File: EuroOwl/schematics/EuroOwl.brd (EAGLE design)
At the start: 100 x 99.8 mm, 119 parts, among them IC1 QUAD_OPAMPD, IC2 QUAD_OPAMPD, IC3 TL072D, Q900 BC846, Q901 BC846, X1 USBPTH-VERTICAL

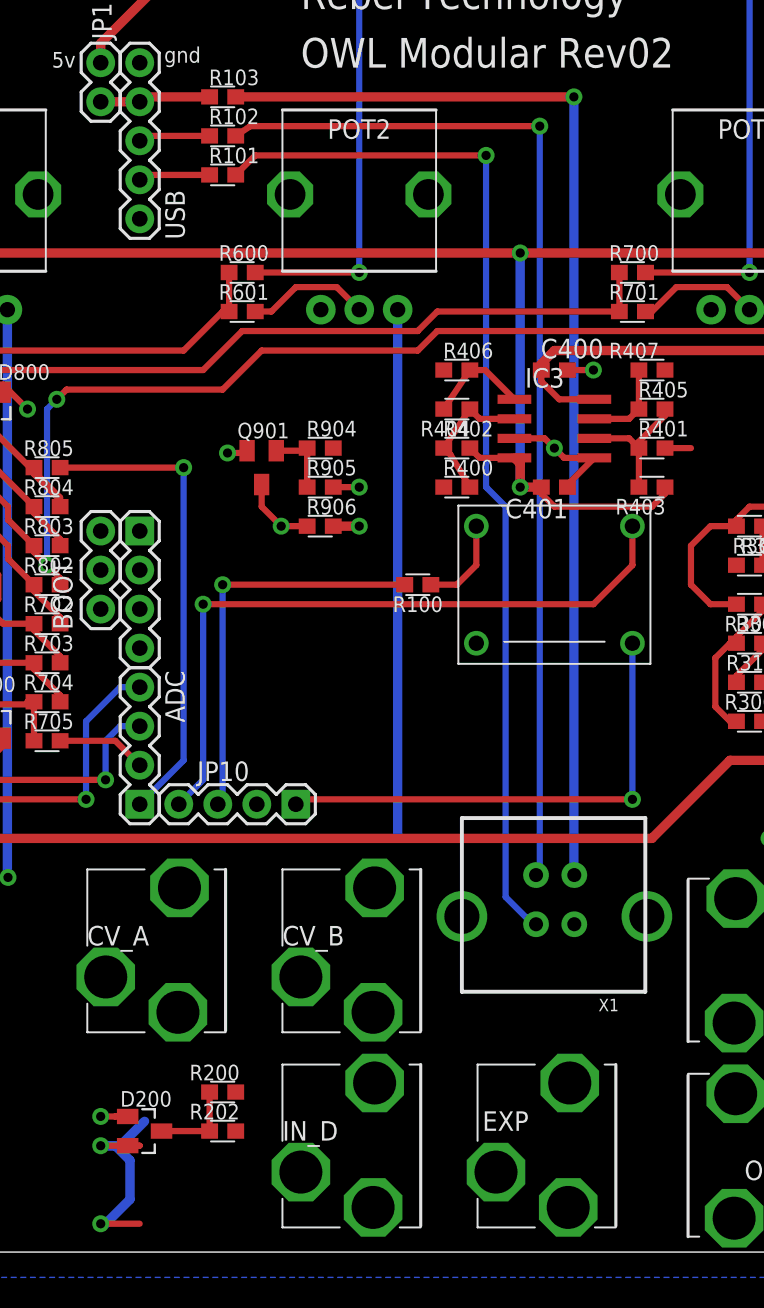
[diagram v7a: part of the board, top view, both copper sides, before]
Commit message: moved USB connector down
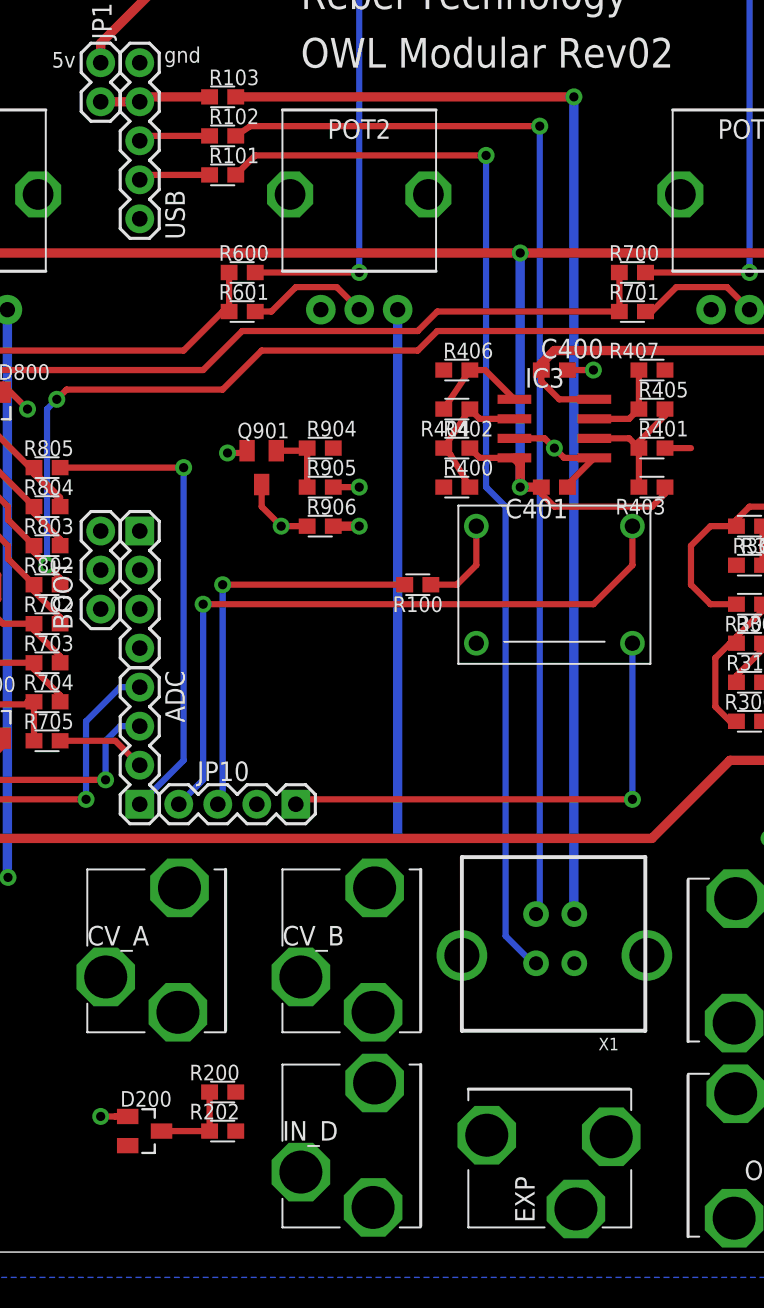
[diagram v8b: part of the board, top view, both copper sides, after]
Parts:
- moved X1 2.54 mm to (50.8, 20.3)
- turned EXP to 90 degrees
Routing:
- net +3V3: track 209.9 -> 193.1 mm, vias 11 -> 9
- net N$52: track 68.8 -> 71.5 mm
- net N$51: track 68.3 -> 70.9 mm
- net N$54: track 72.7 -> 75.2 mm
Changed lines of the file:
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@@
 <element name="OUT_L" library="Rebel" package="CON-LUMBERG_1502_03" value="CON-LUMBERG_1502_03" x="91.44" y="20.32" rot="R180"/>
 <element name="OUT_R" library="Rebel" package="CON-LUMBERG_1502_03" value="CON-LUMBERG_1502_03" x="91.44" y="7.62" rot="R180"/>
-<element name="EXP" library="Rebel" package="CON-LUMBERG_1502_03" value="CON-LUMBERG_1502_03" x="50.8" y="7.62" smashed="yes">
-<attribute name="NAME" x="46.1175" y="8.905" size="1.27" layer="25" font="vector"/>
+<element name="EXP" library="Rebel" package="CON-LUMBERG_1502_03" value="CON-LUMBERG_1502_03" x="50.8" y="7.62" smashed="yes" rot="R90">
+<attribute name="NAME" x="49.515" y="2.9375" size="1.27" layer="25" font="vector" rot="R90"/>
 </element>
 <element name="POT5" library="Rebel" package="POT-ALPS-RK09L1140" value="POT-ALPS-RK09L1140" x="12.7" y="95.25" locked="yes"/>
@@
 <attribute name="NAME" x="78.1685" y="12.192" size="1.016" layer="25"/>
 </element>
-<element name="X1" library="SparkFun" package="USB-B-PTH-VERTICAL" value="USBPTH-VERTICAL" x="50.8" y="22.86"/>
+<element name="X1" library="SparkFun" package="USB-B-PTH-VERTICAL" value="USBPTH-VERTICAL" x="50.8" y="20.32"/>
 <element name="R101" library="Rebel" package="0603" value="22R" x="29.21" y="71.12" smashed="yes">
 <attribute name="NAME" x="28.321" y="71.882" size="1.016" layer="25"/>
@@
 <wire x1="73.72" y1="44.45" x2="73.72" y2="46.99" width="0" layer="19" extent="1-1"/>
 <wire x1="75.88" y1="55.71" x2="71.97" y2="50.8" width="0" layer="19" extent="1-1"/>
-<wire x1="52.0954" y1="22.352" x2="62.6" y2="24.02" width="0" layer="19" extent="1-1"/>
+<wire x1="52.0954" y1="19.812" x2="62.6" y2="24.02" width="0" layer="19" extent="1-1"/>
 <wire x1="62.6" y1="11.32" x2="67.3" y2="21.72" width="0" layer="19" extent="1-1"/>
 <wire x1="90.54" y1="11.32" x2="90.54" y2="24.02" width="0" layer="19" extent="1-1"/>
 <wire x1="80.96" y1="6.52" x2="90.54" y2="11.32" width="0" layer="19" extent="1-1"/>
 <wire x1="77.1525" y1="8.89" x2="80.96" y2="6.52" width="0" layer="19" extent="1-1"/>
-<wire x1="51.7" y1="3.92" x2="62.6" y2="11.32" width="0" layer="19" extent="1-1"/>
-<wire x1="47" y1="6.22" x2="51.7" y2="3.92" width="0" layer="19" extent="1-1"/>
-<wire x1="39" y1="3.92" x2="47" y2="6.22" width="0" layer="19" extent="1-1"/>
+<wire x1="54.5" y1="8.52" x2="62.6" y2="11.32" width="0" layer="19" extent="1-1"/>
+<wire x1="52.2" y1="3.82" x2="54.5" y2="8.52" width="0" layer="19" extent="1-1"/>
+<wire x1="39" y1="3.92" x2="52.2" y2="3.82" width="0" layer="19" extent="1-1"/>
 <wire x1="34.3" y1="6.22" x2="39" y2="3.92" width="0" layer="19" extent="1-1"/>
 <wire x1="39" y1="16.62" x2="34.3" y2="6.22" width="0" layer="19" extent="1-1"/>
@@
 <wire x1="36.41" y1="48.26" x2="38.1" y2="48.26" width="0.6096" layer="1"/>
 <via x="38.1" y="48.26" extent="1-16" drill="0.6"/>
-<wire x1="21.2725" y1="7.9375" x2="22.5425" y2="7.9375" width="0.6096" layer="16"/>
-<wire x1="22.5425" y1="7.9375" x2="24.13" y2="9.525" width="0.6096" layer="16"/>
-<wire x1="23.03" y1="7.94" x2="23.81" y2="7.94" width="0.4064" layer="1"/>
-<wire x1="23.81" y1="7.94" x2="21.2725" y2="7.9375" width="0.4064" layer="1"/>
-<via x="21.2725" y="7.9375" extent="1-16" drill="0.6"/>
-<wire x1="23.81" y1="2.86" x2="21.2725" y2="2.8575" width="0.4064" layer="1"/>
-<via x="21.2725" y="2.8575" extent="1-16" drill="0.6"/>
-<wire x1="21.2725" y1="2.8575" x2="21.59" y2="2.8575" width="0.6096" layer="16"/>
-<wire x1="21.59" y1="2.8575" x2="23.1775" y2="4.445" width="0.6096" layer="16"/>
-<wire x1="23.1775" y1="4.445" x2="23.1775" y2="6.985" width="0.6096" layer="16"/>
-<wire x1="23.1775" y1="6.985" x2="22.225" y2="7.9375" width="0.6096" layer="16"/>
-<wire x1="22.225" y1="7.9375" x2="21.2725" y2="7.9375" width="0.6096" layer="16"/>
 <wire x1="94.9325" y1="78.4225" x2="94.645" y2="78.74" width="0.6096" layer="1"/>
 <wire x1="94.645" y1="78.74" x2="90.2" y2="78.74" width="0.6096" layer="1"/>
@@
 <wire x1="21.2725" y1="47.9425" x2="13.02" y2="56.98" width="0" layer="19" extent="1-1"/>
 <wire x1="36.41" y1="48.26" x2="21.2725" y2="47.9425" width="0" layer="19" extent="1-1"/>
-<wire x1="21.2725" y1="7.9375" x2="8.89" y2="27.94" width="0" layer="19" extent="16-16"/>
+<wire x1="23.03" y1="7.94" x2="8.89" y2="27.94" width="0" layer="19" extent="1-16"/>
 </signal>
 <signal name="PA3">
@@
 <contactref element="EXP" pad="P$2"/>
 <contactref element="R200" pad="1"/>
-<wire x1="30.06" y1="11.43" x2="51.8" y2="12.02" width="0" layer="19" extent="1-1"/>
+<wire x1="30.06" y1="11.43" x2="46.4" y2="8.62" width="0" layer="19" extent="1-1"/>
 </signal>
 <signal name="N$48">
@@
 <contactref element="X1" pad="D+"/>
 <contactref element="R101" pad="2"/>
-<wire x1="49.6062" y1="22.352" x2="49.403" y2="22.352" width="0.4064" layer="16"/>
-<wire x1="49.403" y1="22.352" x2="47.625" y2="24.13" width="0.4064" layer="16"/>
-<wire x1="47.625" y1="24.13" x2="47.625" y2="49.53" width="0.4064" layer="16"/>
+<wire x1="49.6062" y1="19.812" x2="49.403" y2="19.812" width="0.4064" layer="16"/>
+<wire x1="49.403" y1="19.812" x2="47.625" y2="21.59" width="0.4064" layer="16"/>
+<wire x1="47.625" y1="21.59" x2="47.625" y2="49.53" width="0.4064" layer="16"/>
 <wire x1="47.625" y1="49.53" x2="46.355" y2="50.8" width="0.4064" layer="16"/>
 <wire x1="46.355" y1="50.8" x2="46.355" y2="72.39" width="0.4064" layer="16"/>
@@
 <contactref element="X1" pad="D-"/>
 <contactref element="R102" pad="2"/>
-<wire x1="49.6062" y1="25.5524" x2="49.6062" y2="25.7937" width="0.4064" layer="16"/>
-<wire x1="49.6062" y1="25.7937" x2="49.8475" y2="26.035" width="0.4064" layer="16"/>
-<wire x1="49.8475" y1="26.035" x2="49.8475" y2="74.295" width="0.4064" layer="16"/>
+<wire x1="49.6062" y1="23.0124" x2="49.6062" y2="22.9362" width="0.4064" layer="16"/>
+<wire x1="49.6062" y1="22.9362" x2="49.8475" y2="23.1775" width="0.4064" layer="16"/>
+<wire x1="49.8475" y1="23.1775" x2="49.8475" y2="74.295" width="0.4064" layer="16"/>
 <via x="49.8475" y="74.295" extent="1-16" drill="0.6"/>
 <wire x1="49.8475" y1="74.295" x2="31.0125" y2="74.295" width="0.4064" layer="1"/>
@@
 <contactref element="R103" pad="2"/>
 <via x="52.07" y="76.2" extent="1-16" drill="0.6"/>
-<wire x1="52.07" y1="76.2" x2="52.07" y2="25.8445" width="0.6096" layer="16"/>
-<wire x1="52.07" y1="25.8445" x2="52.0954" y2="25.5524" width="0.6096" layer="16"/>
+<wire x1="52.07" y1="76.2" x2="52.07" y2="23.3045" width="0.6096" layer="16"/>
+<wire x1="52.07" y1="23.3045" x2="52.0954" y2="23.0124" width="0.6096" layer="16"/>
 <wire x1="52.07" y1="76.2" x2="30.06" y2="76.2" width="0.6096" layer="1"/>
 </signal>
